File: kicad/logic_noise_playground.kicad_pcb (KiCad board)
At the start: 2 copper layers, 200 x 100 mm, 160 parts, among them J1 JACK_TRS_6PINS, P1 CONN_02X03, P10 CONN_01X03, P11 CONN_01X05, P12 CONN_02X04, P13 CONN_01X03, P14 CONN_01X02, P15 CONN_02X08, P16 CONN_01X04, P17 CONN_02X04, P18 CONN_01X04, P19 CONN_01X02, P2 CONN_01X02, P20 CONN_01X06, P21 CONN_02X03, P22 CONN_02X03, P23 CONN_01X02, P24 CONN_02X01, P25 CONN_01X02, P26 CONN_02X12, P27 CONN_01X02, P28 CONN_01X02, P29 CONN_01X02, P3 CONN_02X02, P30 CONN_01X02, P31 CONN_01X02, P32 CONN_01X03, P33 CONN_01X04, P34 CONN_01X04, P35 CONN_01X04, P36 CONN_01X04, P37 CONN_02X01, P38 CONN_01X04, P39 CONN_01X04, P4 CONN_02X06, P40 CONN_01X02, P5 CONN_02X02, P6 4017 Outs, P7 CONN_01X08, P8 CONN_02X03, P9 CONN_01X08, Q1 LM3904, SW1 Set, SW2 Clear, U1 40106, U2 4070, U3 40106, U4 4069, U5 4051, U6 4015, U7 4017, U8 4040

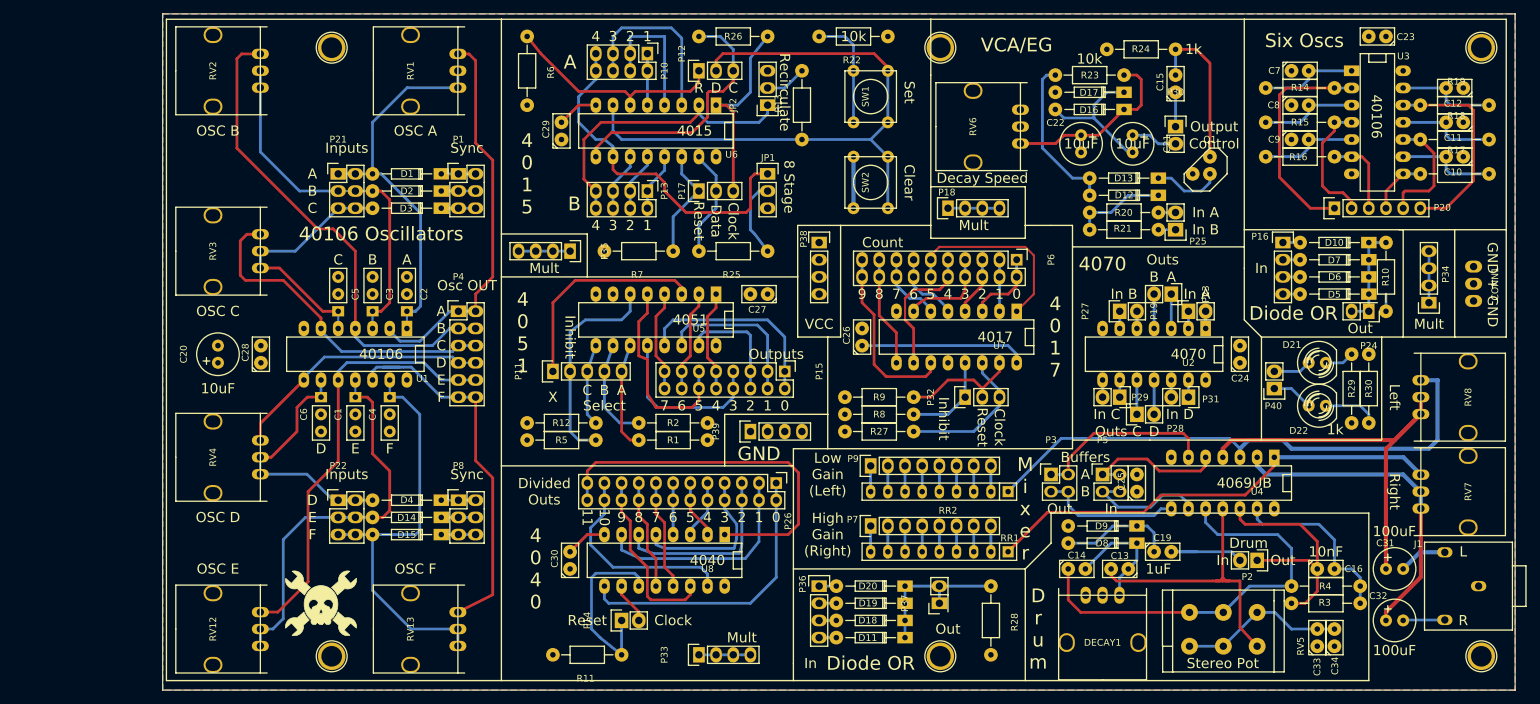
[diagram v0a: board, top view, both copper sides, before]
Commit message: fix vcc and grounding
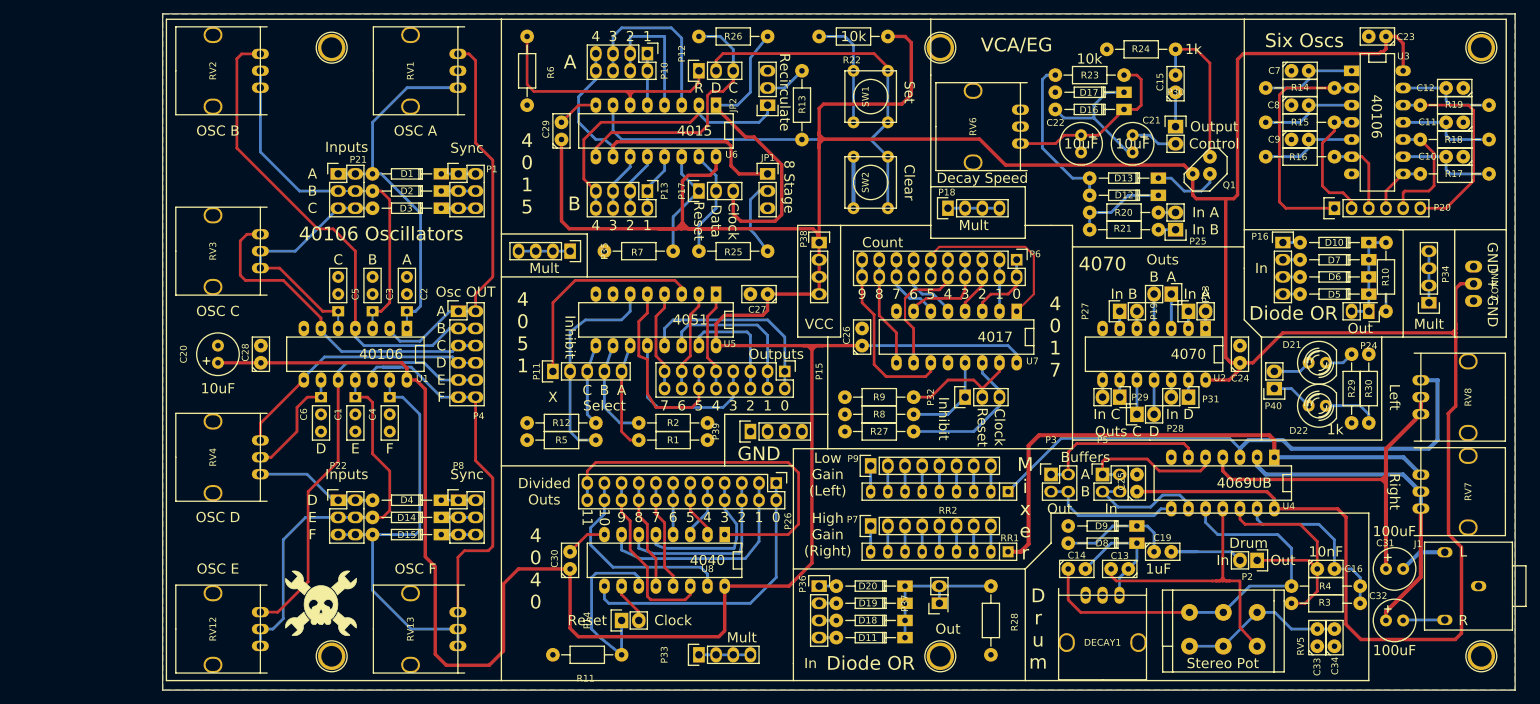
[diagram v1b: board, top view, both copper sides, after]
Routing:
- net VCC: track 24.7 -> 705.1 mm
- net /4015/ClockB: track 29.7 -> 47.3 mm
- net /bass_drum/Buffer_A_In: track 68.6 -> 80.6 mm
- net /4015/ResetA: track 33.1 -> 40.3 mm
- net /4015/4A: track 52.1 -> 47.7 mm
- net /bass_drum/Buffer_B_Out: track 60.2 -> 57.1 mm
- net /six_oscs/out_A: track 33.3 -> 35.4 mm
- net /bass_drum/OD_A_OUT: track 27.3 -> 25.8 mm
- net /bass_drum/OD_A_IN: track 21.0 -> 22.2 mm
- net /40106_oscillators/OutF: track 57.7 -> 58.7 mm
- net /4015/ClockA: track 38.3 -> 38.9 mm
- net Net-(JP2-Pad2): vias 1 -> 0
- added copper zone on F.Cu, net GND
- removed copper zone on F.Cu, net VCC

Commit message: update part numbers
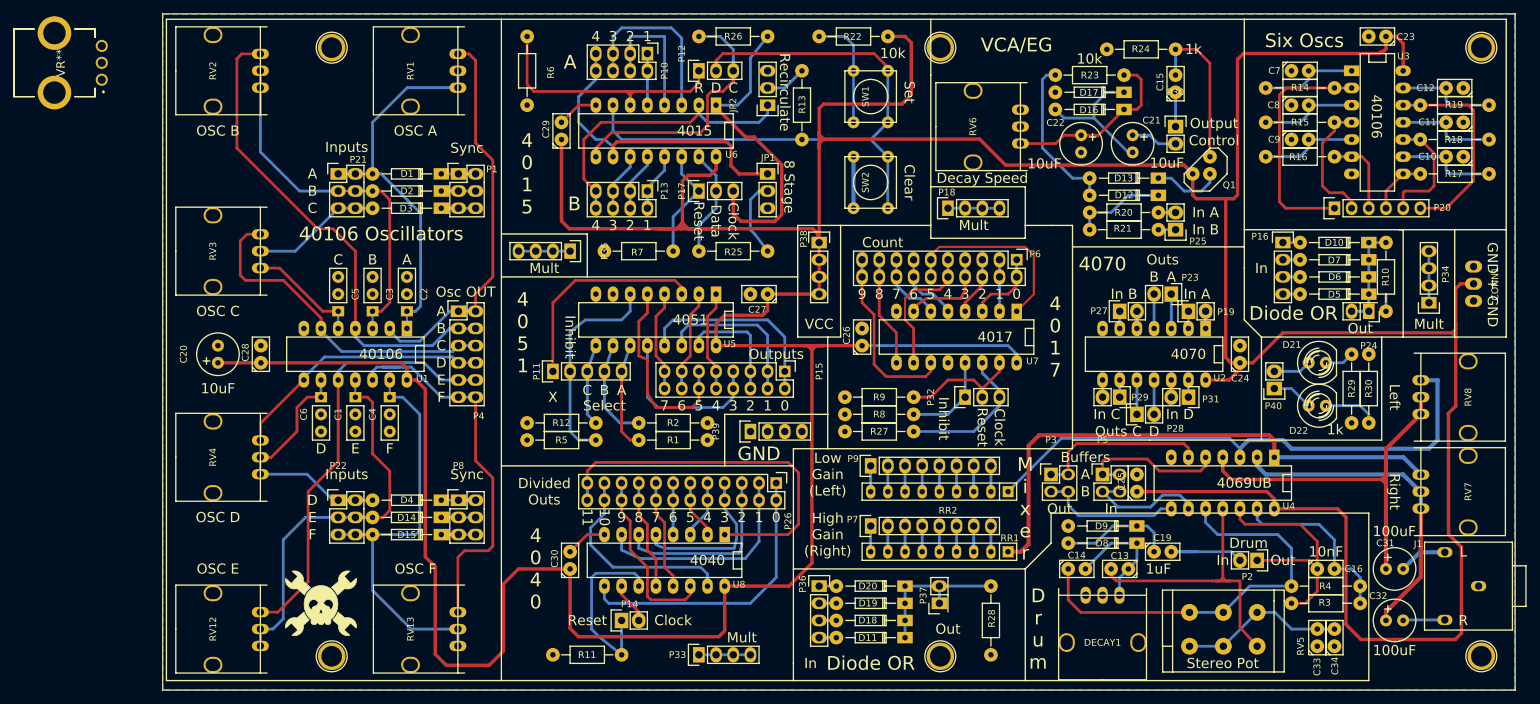
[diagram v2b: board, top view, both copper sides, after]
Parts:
- added VR**: PTV09A4025FB104, logic_noise:PTV09A4025FB104, F.Cu at (26.0, 59.7)

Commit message: update traces
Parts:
- moved VR** 7.56 mm to (33.5, 61.0)
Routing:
- net /40106_oscillators/InA: track 59.3 -> 70.0 mm
- net /40106_oscillators/OutB: track 72.9 -> 81.9 mm
- net /bass_drum/Buffer_B_In: track 82.9 -> 89.5 mm
- net /40106_oscillators/OutE: track 65.1 -> 71.4 mm
- net GND: track 22.4 -> 16.3 mm
- net Net-(C21-Pad2): track 21.2 -> 26.5 mm
- net /40106_oscillators/OutD: track 39.0 -> 43.7 mm
- net /bass_drum/Buffer_A_Out: track 48.2 -> 51.8 mm
- net /4040/Reset: track 27.3 -> 24.1 mm
- net /40106_oscillators/InC: track 38.4 -> 41.5 mm
- net /4015/ClockB: track 47.3 -> 50.3 mm
- net /40106_oscillators/InD: track 38.0 -> 40.9 mm
- net /40106_oscillators/InF: track 63.3 -> 66.0 mm
- net Net-(JP1-Pad2): track 11.6 -> 14.3 mm
- net /4017/Clock: track 21.7 -> 24.3 mm
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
